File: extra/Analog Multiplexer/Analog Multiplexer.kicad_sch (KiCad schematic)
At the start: 12 parts, among them J1 Conn_01x05_Socket, J2 Conn_01x05_Socket, J3 Conn_01x05_Socket, J4 Conn_01x05_Socket, J5 Conn_01x05_Socket, J6 Conn_01x04_Socket, U1 TLV1117-33, U4 ADG729, U5 ADG729

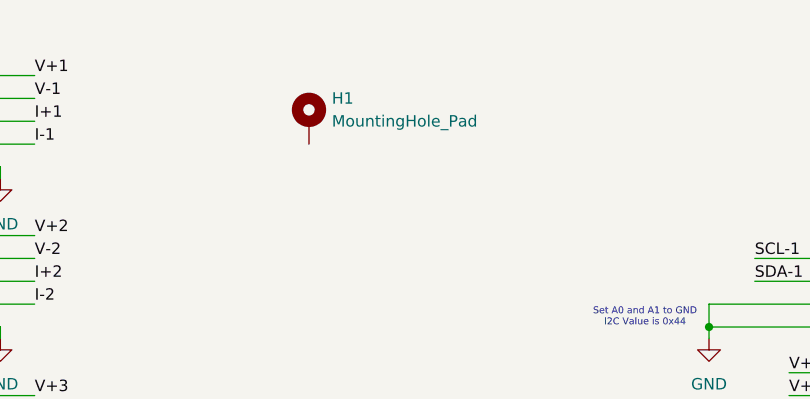
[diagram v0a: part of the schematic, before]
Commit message: Bypass caps and I2C Header changed
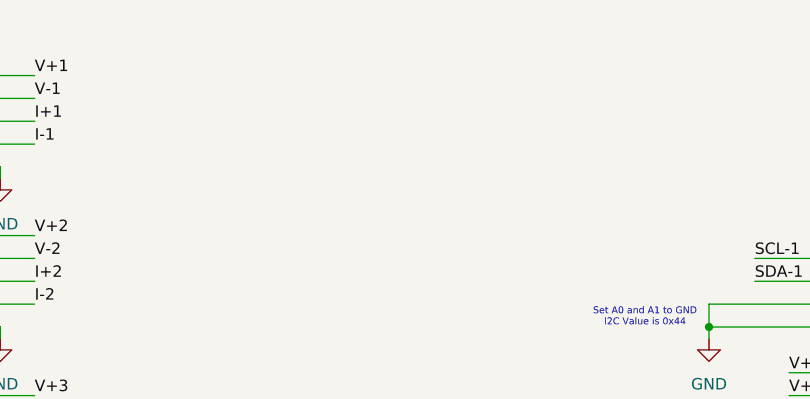
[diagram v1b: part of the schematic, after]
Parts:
- removed H1: MountingHole_Pad, MountingHole:MountingHole_3mm_Pad, symbol Mechanical:MountingHole_Pad
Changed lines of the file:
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@@
-	)
-	(symbol
-		(lib_id "Mechanical:MountingHole_Pad")
-		(at 68.58 22.86 0)
-		(unit 1)
-		(exclude_from_sim no)
-		(in_bom no)
-		(on_board yes)
-		(dnp no)
-		(fields_autoplaced yes)
-		(property "Reference" "H1"
-			(at 71.12 20.3199 0)
-			(effects
-				(font
-					(size 1.27 1.27)
-				)
-				(justify left)
-			)
-		)
-		(property "Value" "MountingHole_Pad"
-			(at 71.12 22.8599 0)
-			(effects
-				(font
-					(size 1.27 1.27)
-				)
-				(justify left)
-			)
-		)
-		(property "Footprint" "MountingHole:MountingHole_3mm_Pad"
-			(at 68.58 22.86 0)
-			(effects
-				(font
-					(size 1.27 1.27)
-				)
-				(hide yes)
-			)
-		)
-		(property "Datasheet" "~"
-			(at 68.58 22.86 0)
-			(effects
-				(font
-					(size 1.27 1.27)
-				)
-				(hide yes)
-			)
-		)
-		(property "Description" "Mounting Hole with connection"
-			(at 68.58 22.86 0)
-			(effects
-				(font
-					(size 1.27 1.27)
-				)
-				(hide yes)
-			)
-		)
-		(pin "1"
-		)
-		(instances
-			(project ""
-				(path "/07b96713-4dcc-47be-89cb-186dda536ea4"
-					(reference "H1")
-					(unit 1)
-				)
-			)
-		)
 	)
 	(symbol

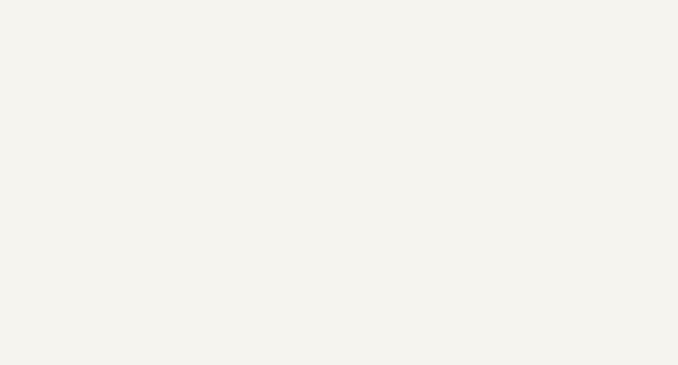
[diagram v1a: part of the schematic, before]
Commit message: Cleaned and added mounting holes
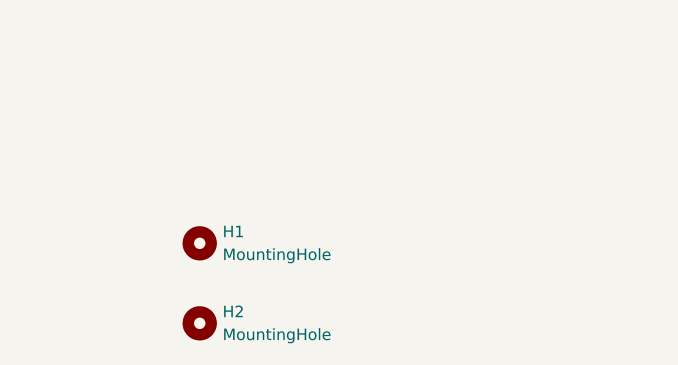
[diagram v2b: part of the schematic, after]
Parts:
- added H1, H2: MountingHole, MountingHole:MountingHole_3.2mm_M3_ISO7380, symbol Mechanical:MountingHole
- J6: MPN (none) -> C160404
- U4, U5: MPN (none) -> C207556
